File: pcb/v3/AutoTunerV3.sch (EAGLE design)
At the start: 113 parts, among them IC2 317EMP, Q1 32,768kHz, Q2 BSS123, Q3 BSS84, U1 TPS63070RNMR, Y1 8MHz

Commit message: board v3 improvements
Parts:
- added D1: (no value), diode:DIODE-SOD323-R
- R32: value 100 -> 60
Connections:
- net N$54: now also D1.A
- net N$55: now also D1.C
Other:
- moved on the sheet: BUZZER, R34
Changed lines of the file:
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@@
 <part name="R30" library="rcl" library_urn="urn:adsk.eagle:library:334" deviceset="R-EU_" device="R0805" package3d_urn="urn:adsk.eagle:package:23553/2" value="100"/>
 <part name="R31" library="rcl" library_urn="urn:adsk.eagle:library:334" deviceset="R-EU_" device="R0805" package3d_urn="urn:adsk.eagle:package:23553/2" value="100"/>
-<part name="R32" library="rcl" library_urn="urn:adsk.eagle:library:334" deviceset="R-EU_" device="R0805" package3d_urn="urn:adsk.eagle:package:23553/2" value="100"/>
+<part name="R32" library="rcl" library_urn="urn:adsk.eagle:library:334" deviceset="R-EU_" device="R0805" package3d_urn="urn:adsk.eagle:package:23553/2" value="60"/>
 <part name="GND37" library="supply1" library_urn="urn:adsk.eagle:library:371" deviceset="GND" device=""/>
 <part name="OPV" library="IC_Linear" library_urn="urn:adsk.eagle:library:16378340" deviceset="LM324" device="_SOIC" package3d_urn="urn:adsk.eagle:package:16378323/2" value="">
@@
 <part name="MOTOR" library="con-molex" library_urn="urn:adsk.eagle:library:165" deviceset="22-?-02" device="27-2021" package3d_urn="urn:adsk.eagle:package:8078645/1" value=""/>
 <part name="R18" library="rcl" library_urn="urn:adsk.eagle:library:334" deviceset="R-EU_" device="R0805" package3d_urn="urn:adsk.eagle:package:23553/2" value="0"/>
+<part name="D1" library="diode" library_urn="urn:adsk.eagle:library:210" deviceset="DIODE-" device="SOD323-R" package3d_urn="urn:adsk.eagle:package:43437/1">
+<attribute name="LCSC_PART" value="C2128"/>
+</part>
 </parts>
 <sheets>
@@
 <wire x1="213.36" y1="38.1" x2="213.36" y2="81.28" width="0.2032" layer="98" style="shortdash"/>
 <wire x1="213.36" y1="81.28" x2="172.72" y2="81.28" width="0.2032" layer="98" style="shortdash"/>
-<wire x1="91.44" y1="124.46" x2="91.44" y2="50.8" width="0.2032" layer="98" style="shortdash"/>
+<wire x1="91.44" y1="129.54" x2="91.44" y2="50.8" width="0.2032" layer="98" style="shortdash"/>
 <wire x1="91.44" y1="50.8" x2="142.24" y2="50.8" width="0.2032" layer="98" style="shortdash"/>
-<wire x1="142.24" y1="50.8" x2="142.24" y2="124.46" width="0.2032" layer="98" style="shortdash"/>
-<wire x1="142.24" y1="124.46" x2="91.44" y2="124.46" width="0.2032" layer="98" style="shortdash"/>
+<wire x1="142.24" y1="50.8" x2="142.24" y2="129.54" width="0.2032" layer="98" style="shortdash"/>
+<wire x1="142.24" y1="129.54" x2="91.44" y2="129.54" width="0.2032" layer="98" style="shortdash"/>
 <text x="101.6" y="53.34" size="2.54" layer="98">Buzzer</text>
 </plain>
@@
 </instance>
 <instance part="T1" gate="G$1" x="129.54" y="78.74" smashed="yes">
-<attribute name="NAME" x="119.38" y="86.36" size="1.778" layer="95"/>
+<attribute name="NAME" x="127" y="81.28" size="1.778" layer="95"/>
 <attribute name="VALUE" x="119.38" y="83.82" size="1.778" layer="96"/>
 <attribute name="LCSC_PART" x="129.54" y="78.74" size="1.778" layer="96" display="off"/>
@@
 <attribute name="VALUE" x="115.57" y="75.438" size="1.778" layer="96"/>
 </instance>
-<instance part="R34" gate="G$1" x="132.08" y="104.14" smashed="yes" rot="R90">
-<attribute name="NAME" x="130.5814" y="100.33" size="1.778" layer="95" rot="R90"/>
-<attribute name="VALUE" x="135.382" y="100.33" size="1.778" layer="96" rot="R90"/>
-</instance>
-<instance part="BUZZER" gate="G$1" x="132.08" y="91.44" smashed="yes" rot="R270">
-<attribute name="NAME" x="138.43" y="95.25" size="1.778" layer="95" rot="R270"/>
-<attribute name="VALUE" x="128.905" y="95.25" size="1.778" layer="96" rot="R270"/>
+<instance part="R34" gate="G$1" x="132.08" y="109.22" smashed="yes" rot="R90">
+<attribute name="NAME" x="130.5814" y="105.41" size="1.778" layer="95" rot="R90"/>
+<attribute name="VALUE" x="135.382" y="105.41" size="1.778" layer="96" rot="R90"/>
+</instance>
+<instance part="BUZZER" gate="G$1" x="132.08" y="93.98" smashed="yes" rot="R270">
+<attribute name="NAME" x="138.43" y="97.79" size="1.778" layer="95" rot="R270"/>
+<attribute name="VALUE" x="128.905" y="97.79" size="1.778" layer="96" rot="R270"/>
 </instance>
 <instance part="GND7" gate="1" x="132.08" y="66.04" smashed="yes">
@@
 <instance part="MOTOR" gate="-2" x="226.06" y="109.22" smashed="yes" rot="R180">
 <attribute name="NAME" x="223.52" y="109.982" size="1.524" layer="95" rot="R180"/>
+</instance>
+<instance part="D1" gate="G$1" x="121.92" y="93.98" smashed="yes" rot="R90">
+<attribute name="NAME" x="121.4374" y="96.52" size="1.778" layer="95" rot="R90"/>
+<attribute name="VALUE" x="124.2314" y="96.52" size="1.778" layer="96" rot="R90"/>
+<attribute name="LCSC_PART" x="121.92" y="93.98" size="1.778" layer="96" rot="R90" display="off"/>
 </instance>
 </instances>
@@
 <segment>
 <pinref part="R34" gate="G$1" pin="2"/>
-<wire x1="132.08" y1="109.22" x2="132.08" y2="111.76" width="0.1524" layer="91"/>
-<label x="132.08" y="111.76" size="1.27" layer="95" rot="R90" xref="yes"/>
+<wire x1="132.08" y1="114.3" x2="132.08" y2="116.84" width="0.1524" layer="91"/>
+<label x="132.08" y="116.84" size="1.27" layer="95" rot="R90" xref="yes"/>
 </segment>
 </net>
@@
 <pinref part="BUZZER" gate="G$1" pin="2"/>
 <wire x1="132.08" y1="83.82" x2="132.08" y2="86.36" width="0.1524" layer="91"/>
+<wire x1="132.08" y1="86.36" x2="132.08" y2="88.9" width="0.1524" layer="91"/>
+<wire x1="132.08" y1="86.36" x2="121.92" y2="86.36" width="0.1524" layer="91"/>
+<junction x="132.08" y="86.36"/>
+<pinref part="D1" gate="G$1" pin="A"/>
+<wire x1="121.92" y1="86.36" x2="121.92" y2="91.44" width="0.1524" layer="91"/>
 </segment>
 </net>
@@
 <pinref part="BUZZER" gate="G$1" pin="1"/>
 <pinref part="R34" gate="G$1" pin="1"/>
-<wire x1="132.08" y1="96.52" x2="132.08" y2="99.06" width="0.1524" layer="91"/>
-</segment>
-</net>
+<wire x1="132.08" y1="99.06" x2="132.08" y2="101.6" width="0.1524" layer="91"/>
+<pinref part="D1" gate="G$1" pin="C"/>
+<wire x1="132.08" y1="101.6" x2="132.08" y2="104.14" width="0.1524" layer="91"/>
+<wire x1="121.92" y1="96.52" x2="121.92" y2="101.6" width="0.1524" layer="91"/>
+<wire x1="121.92" y1="101.6" x2="132.08" y2="101.6" width="0.1524" layer="91"/>
+<junction x="132.08" y="101.6"/>
+</segment>
+</net>

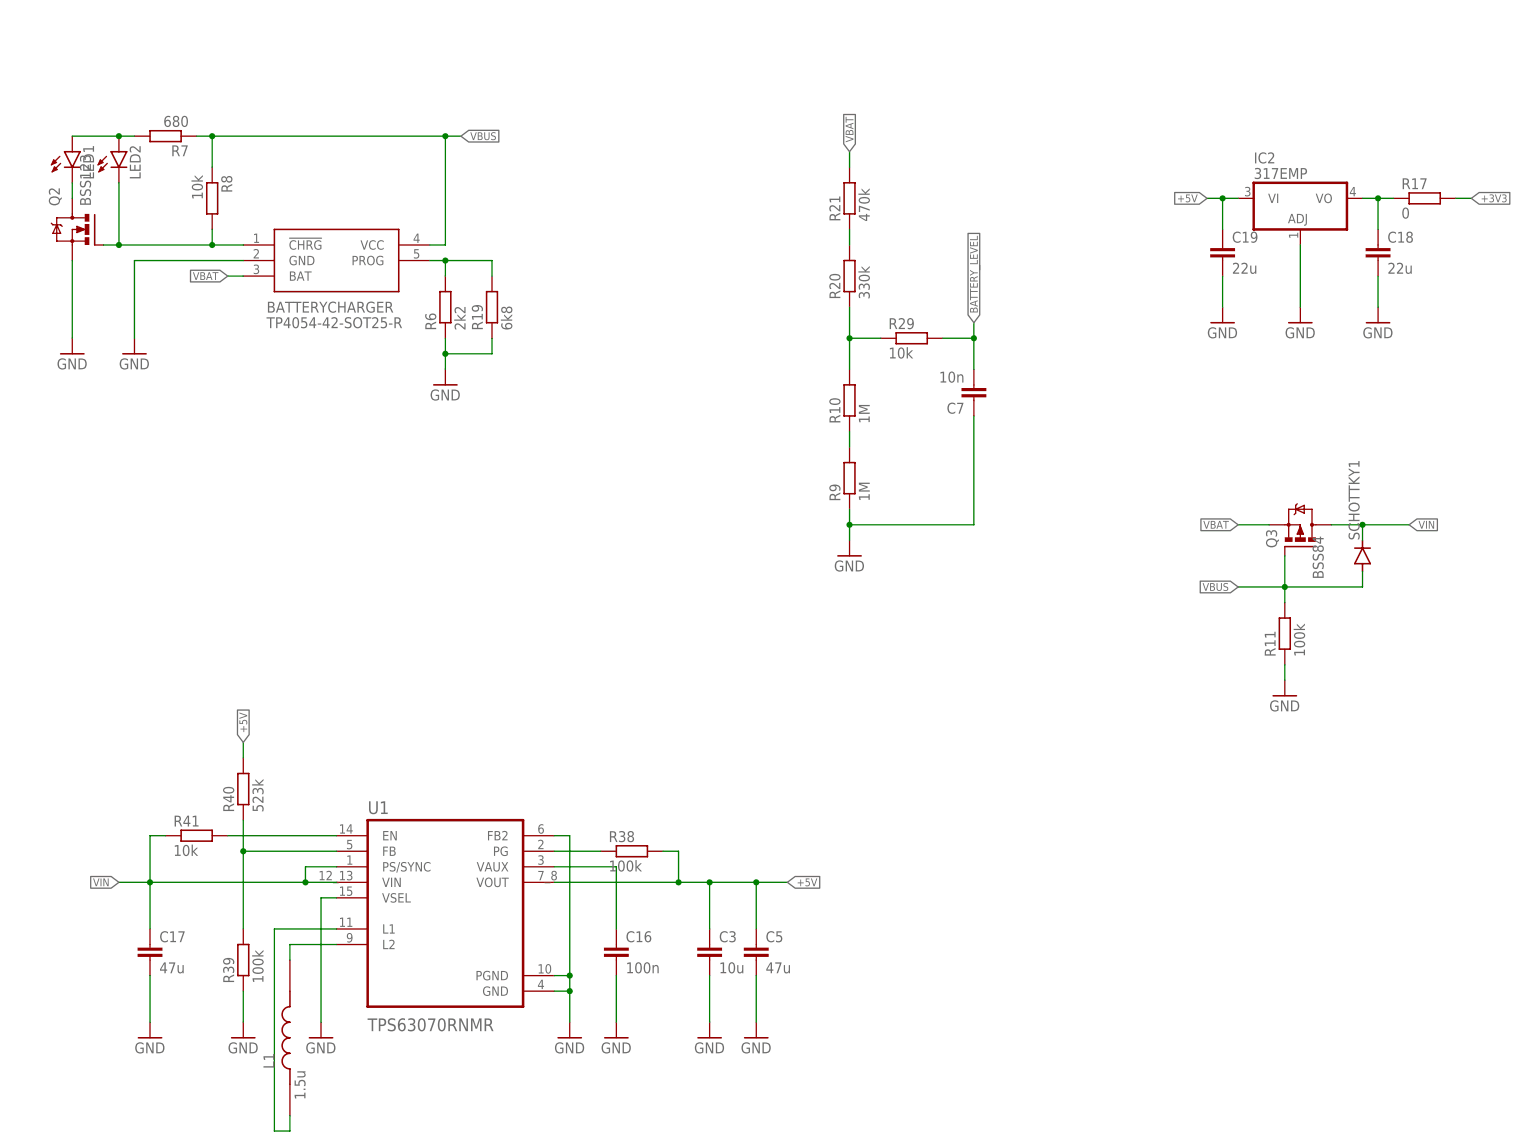
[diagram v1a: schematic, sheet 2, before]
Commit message: board v3 dcdc design change
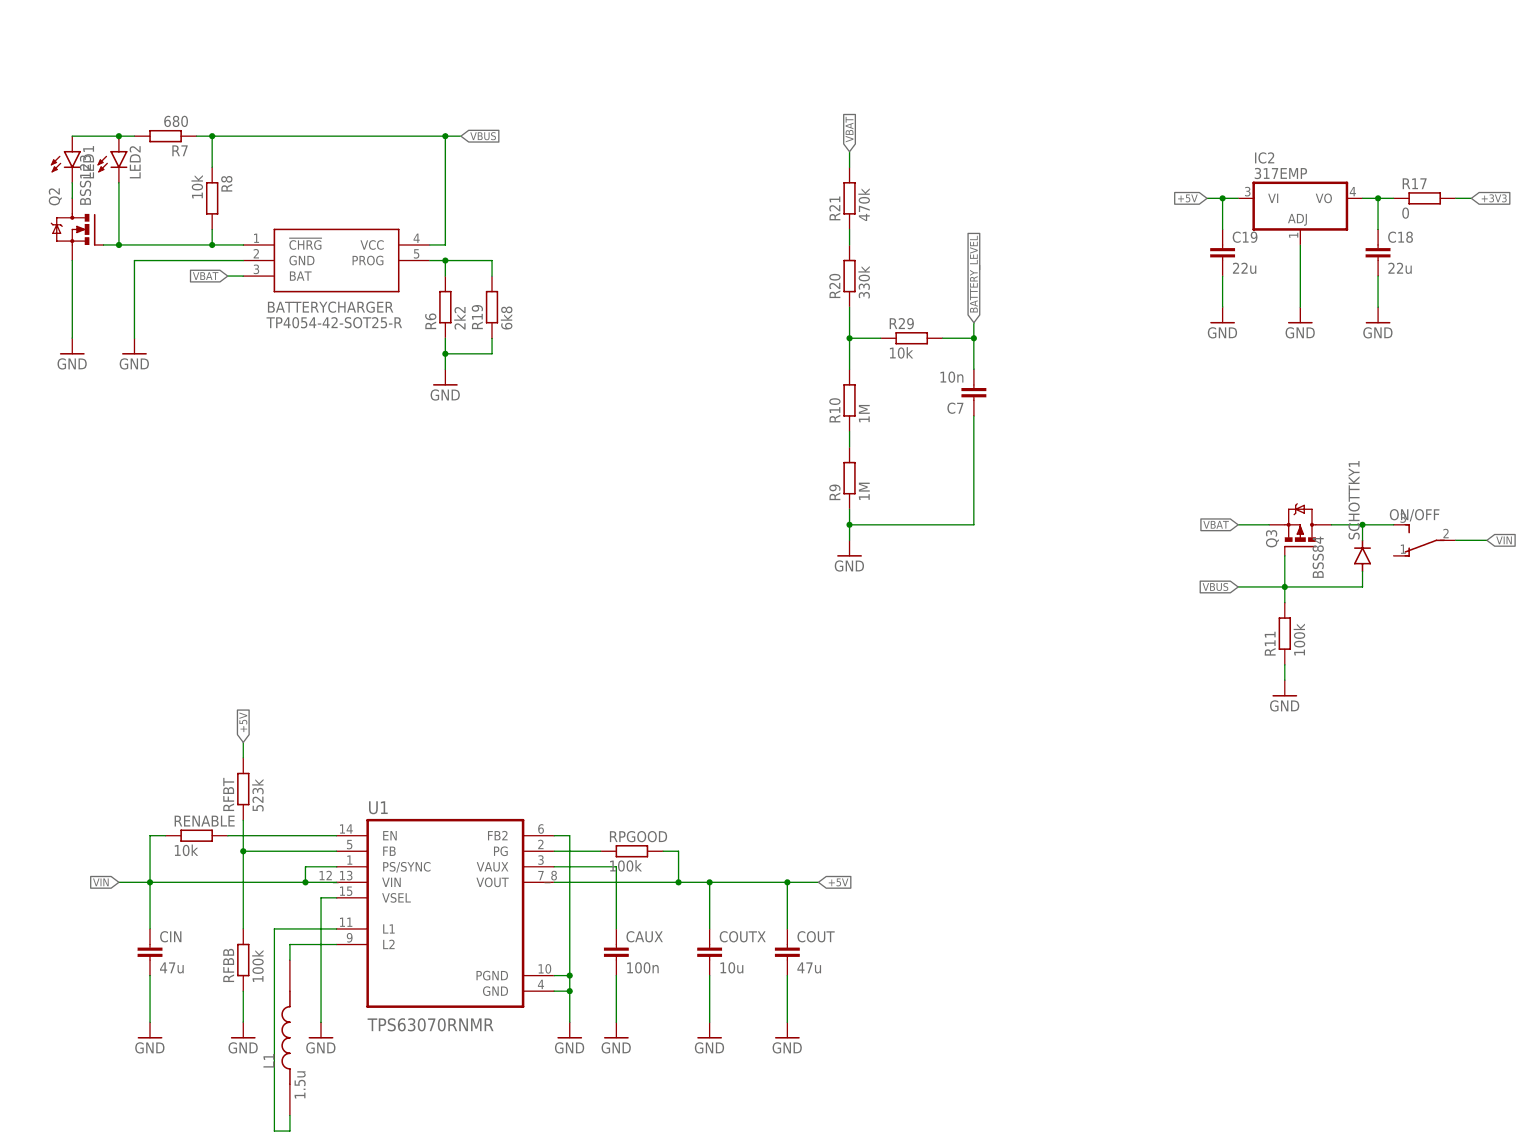
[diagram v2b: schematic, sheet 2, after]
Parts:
- removed C16: 100n, rcl:C-EUC0805
- removed C17, C5: 47u, rcl:C-EUC0805
- removed C3: 10u, rcl:C-EUC0805
- added CAUX: 100n, rcl:C-EUC0402
- added CIN, COUT: 47u, rcl:C-EUC1206
- added COUTX: 10u, rcl:C-EUC0603
- added ON/OFF: TL36PO, switch:TL36PO
- renumbered R38 to RPGOOD, R39 to RFBB, R40 to RFBT, R41 to RENABLE
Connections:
- net N$58 renamed L2
- net N$59 renamed L1
- removed net N$45: R18.2, STM32.PA2
- new net N$3: ON/OFF.S, Q3.D, SCHOTTKY1.C
- new net N$7: OPV.OUT3, R18.1, R27.1
- net +5V: now also COUT.1, COUTX.1; no longer C3.1, C5.1
- net GND: now also CAUX.2, CIN.2, COUT.2, COUTX.2; no longer C16.2, C17.2, C3.2, C5.2
- net N$60: now also CAUX.1; no longer C16.1
- net SIGNAL_OPAMP: now also R18.2, STM32.PA2; no longer OPV.OUT3, R18.1, R27.1
- net VIN: now also CIN.1, ON/OFF.P; no longer C17.1, Q3.D, SCHOTTKY1.C

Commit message: board v3 finished
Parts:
- removed LED5, LED6: (no value), led:LEDCHIP-LED0805
- added LED_CHARGE_GREEN, LED_CHARGE_RED: (no value), led:LEDCHIPLED_0805
- C18, C19: LCSC_PART C5672 -> C12891
- LED1: device led:LEDCHIPLED_0805 -> led:LEDCHIP-LED0805
- LED2: device led:LEDCHIPLED_0805 -> led:LEDCHIP-LED0805; LCSC_PART C84256 -> C2297
- LED3, LED4: LCSC_PART (none) -> C2297
- LED_INDICATOR: LCSC_PART C84256 -> C2296
- R1: LCSC_PART C17802 -> C17557
- R32: value 60 -> 56
- renumbered C4 to C_H-BRIDGE, D8 to D_H-BRIDGE1, D9 to D_H-BRIDGE2, JP2 to EXTENSIONS, Q1 to QUARTZ2, Q2 to N-CHANNEL, Q3 to P-CHANNEL, RED_LED to LED_INDICATOR, T1 to NPN, Y1 to QUARTZ
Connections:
- net GND: now also LED1.C, LED2.C; no longer LED5.C, LED6.C
- net N$11: now also LED_CHARGE_GREEN.A, LED_CHARGE_RED.A; no longer LED1.A, LED2.A
- net N$12: now also LED_CHARGE_GREEN.C; no longer LED1.C
- net N$39: now also LED1.A; no longer LED3.A
- net N$48: now also LED2.A; no longer LED6.A
- net N$49: now also LED3.A; no longer LED4.A
- net N$50: now also LED4.A; no longer LED5.A
- net N$9: now also LED_CHARGE_RED.C; no longer LED2.C
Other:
- moved on the sheet: LED3, LED4

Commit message: settings menu
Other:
- note added: "32kHz Quarz"
- note added: "5V --> 3V3"
- note added: "8MHz Quarz"
- note added: "Audio Jack"
- note added: "Batterie"
- note added: "Battery charger"
- note added: "DC - Motor"
- note added: "DC MOTOR H-Bridge"
- note added: "OPV: Vu = 1,1 - ∞"
- note added: "Power IN"
- note added: "Voltage Source Selection"
- note removed: "32kHz Quarz ok"
- note removed: "5V --> 3V3 ok"
- note removed: "8MHz Quarz ok"
- note removed: "Audio Jack ok"
- note removed: "Batterie ok"
- note removed: "Battery charger ok"
- note removed: "DC - Motor ok"
- note removed: "DC MOTOR H-Bridge ok"
- note removed: "OPV: Vu = 1,1 - ∞ok"
- note removed: "Power IN ok"
- note removed: "Voltage Source Selection ok"
- moved on the sheet: C10, C11, C13, C14, C26, C6, C8, C9, QUARTZ, QUARTZ2, R12, R37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
